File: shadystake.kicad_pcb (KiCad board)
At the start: 2 copper layers, 129.5 x 76.2 mm, 15 parts, among them J1 6P6C, J2 6P6C, J3 6P6C, J4 6P6C, J5 6P6C, J6 6P6C, J7 8P8C

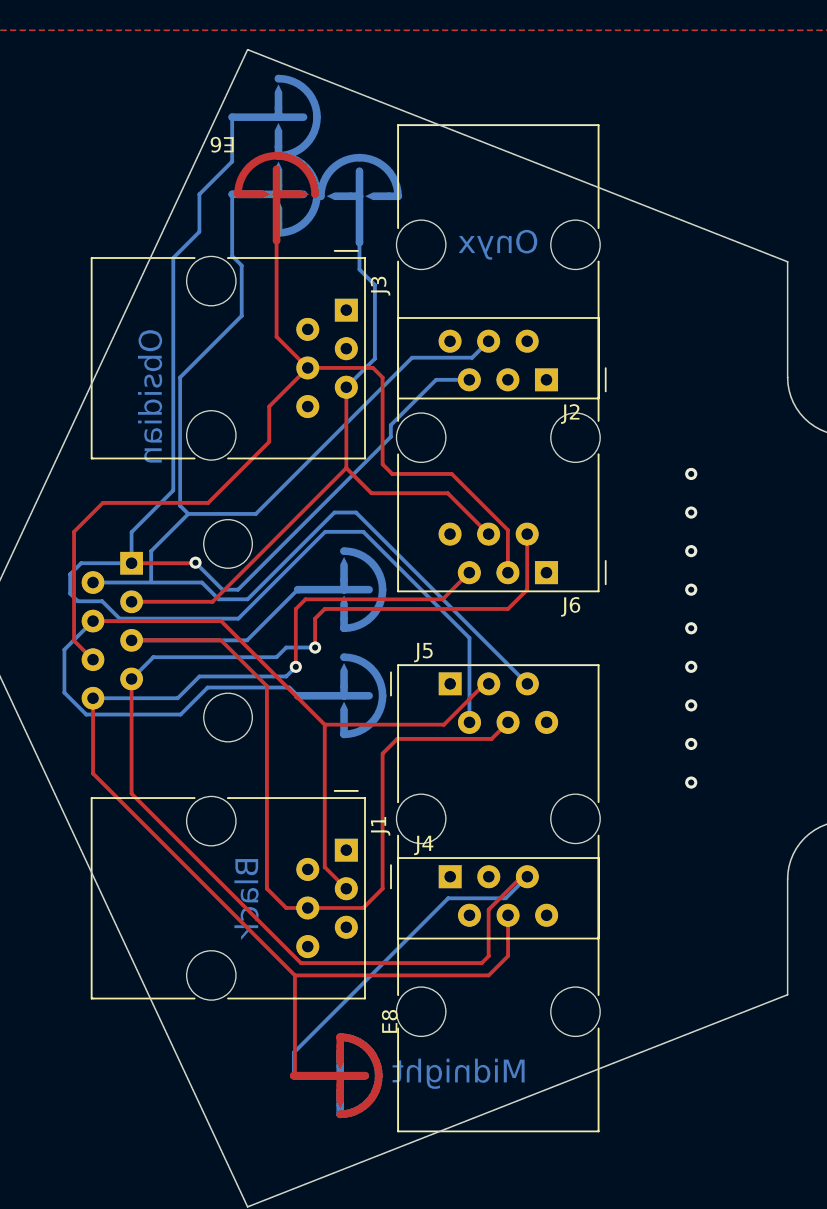
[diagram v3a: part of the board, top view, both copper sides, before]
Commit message: fix spark gaps, continuity on PCB
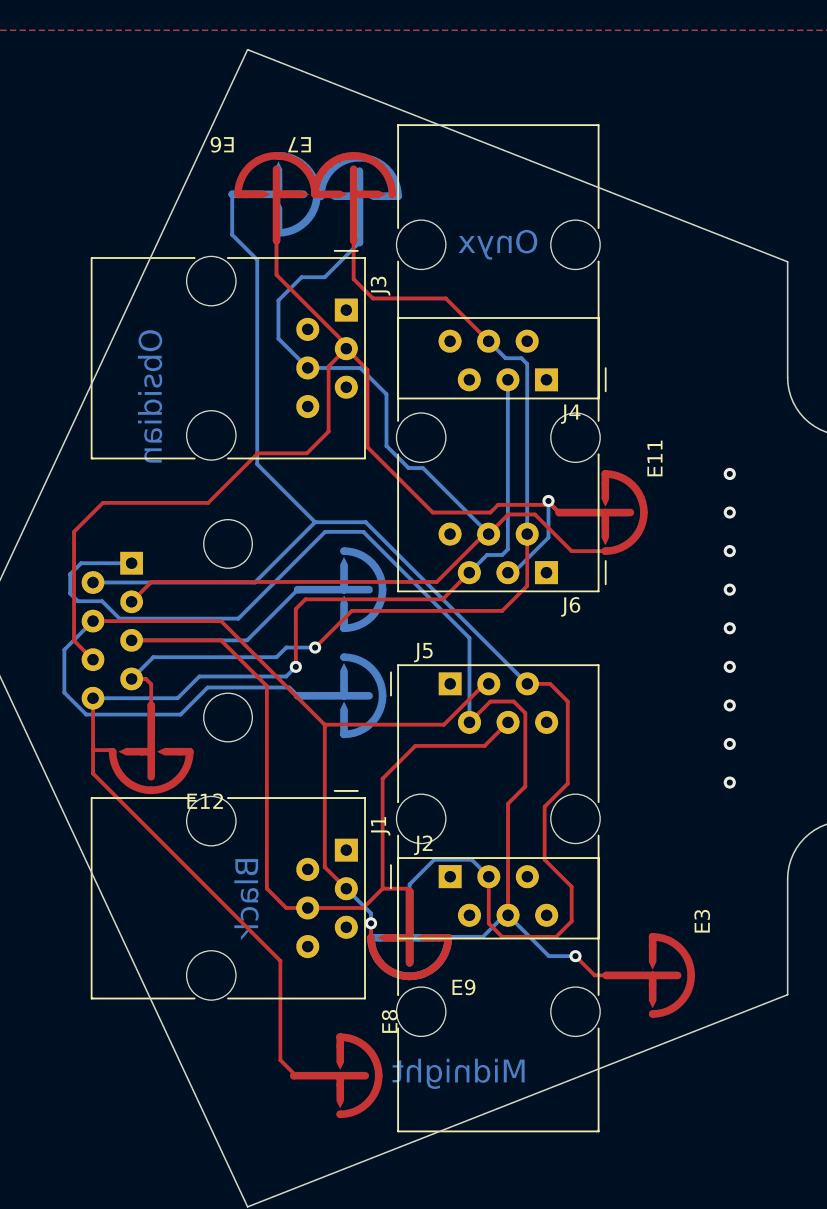
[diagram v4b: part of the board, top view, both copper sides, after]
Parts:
- added E10: SPARK_GAP, Shadystake:Sparkgap_JLC, B.Cu at (76.7, 134.7)
- added E11: SPARK_GAP, Shadystake:Sparkgap_JLC, F.Cu at (89.6, 106.7)
- added E12: SPARK_GAP, Shadystake:Sparkgap_JLC, F.Cu at (59.7, 122.4)
- added E9: SPARK_GAP, Shadystake:Sparkgap_JLC, F.Cu at (76.7, 134.7)
- E3, E7: moved to F.Cu
- moved E3 61.7 mm to (92.7, 137.2), turned to 90 degrees
- moved E7 58.0 mm to (73.0, 85.7), turned to 180 degrees
- moved J2 33.3 mm to (79.4, 130.7), turned to 0 degrees
- moved J4 33.3 mm to (85.7, 97.9), turned to 180 degrees
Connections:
- net GND renamed Earth_Protective
- J2 pad 3: unconnected-(J2-Pad3) -> /RING2
- J2 pad 4: /RING2 -> /TIP2
- J2 pad 5: /TIP2 -> unconnected-(J2-Pad5)
- J3 pad 3: unconnected-(J3-Pad3) -> /RING3
- J3 pad 4: /RING3 -> /TIP3
- J3 pad 5: /TIP3 -> unconnected-(J3-Pad5)
- J4 pad 3: unconnected-(J4-Pad3) -> /RING4
- J4 pad 4: /RING4 -> /TIP4
- J4 pad 5: /TIP4 -> unconnected-(J4-Pad5)
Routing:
- net /TIP4: track 97.0 -> 62.3 mm
- net /TIP2: track 104.7 -> 74.1 mm
- net /TIP3: track 45.0 -> 64.9 mm
- net /RING3: track 63.2 -> 71.7 mm, vias 0 -> 1
- net /RING2: track 89.2 -> 93.6 mm
- net /RING1: track 63.5 -> 67.5 mm, vias 0 -> 1
- net /RING4: track 78.1 -> 76.4 mm
- net /TIP1: track 62.5 -> 63.5 mm

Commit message: Lay out design
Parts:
- E1, E2, E4, E5: footprint Shadystake:Sparkgap_JLC -> Shadystake:Spark_Gap_Teeth; moved to F.Cu
- E10, E3, E6, E7, E8: footprint Shadystake:Sparkgap_JLC -> Shadystake:Spark_Gap_Teeth
- E11, E12, E9: footprint Shadystake:Sparkgap_JLC -> Shadystake:Spark_Gap_Teeth; moved to B.Cu
- J1, J2, J3, J4, J5, J6: footprint Connector_RJ:RJ12_Amphenol_54601 -> Shadystake:6P4C_Vert
- J7: footprint Connector_RJ:RJ45_Amphenol_54602-x08_Horizontal -> Shadystake:8P8C_Hor
- moved E10 104.4 mm to (152.4, 62.7)
- moved J2 103.8 mm to (149.2, 53.9)
- moved J6 98.5 mm to (131.4, 23.4), turned to 0 degrees
- moved E12 98.1 mm to (116.8, 42.7)
- moved J3 97.2 mm to (149.2, 33.6), turned to 0 degrees
- moved J7 91.9 mm to (139.1, 66.0), turned to 180 degrees
- moved J5 90.7 mm to (131.4, 43.7)
- moved E11 89.9 mm to (152.4, 42.4), turned to 180 degrees
- moved J1 85.6 mm to (113.7, 53.9), turned to 0 degrees
- moved E8 84.8 mm to (126.5, 78.7), turned to 0 degrees
- moved E9 82.2 mm to (116.8, 63.0)
- moved E3 76.9 mm to (142.7, 78.7), turned to 180 degrees
- moved E2 74.8 mm to (135.6, 78.7), turned to 0 degrees
- moved E4 72.5 mm to (140.2, 78.7), turned to 0 degrees
- moved J4 70.2 mm to (113.7, 33.6), turned to 0 degrees
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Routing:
- net /RING2: track 93.6 -> 62.7 mm
- net /RING1: track 67.5 -> 84.9 mm, vias 1 -> 0
- net /TIP4: track 62.3 -> 76.7 mm, vias 1 -> 0
- net /TIP1: track 63.5 -> 77.7 mm
- net /TIP3: track 64.9 -> 76.2 mm
- net /TIP2: track 74.1 -> 67.0 mm, vias 1 -> 0
- net /RING4: track 76.4 -> 83.2 mm, vias 1 -> 0
- net /RING3: track 71.7 -> 65.3 mm, vias 1 -> 0
- net Earth_Protective: vias 9 -> 0
- removed copper zone on B.Cu, net Earth_Protective
- removed copper zone on F.Cu, net Earth_Protective
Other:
- board size 129.5 x 76.2 mm -> 96.8 x 67.9 mm
- board text added: "EXPOSED COPPER IS A SAFETY FEATURE DANGER: HIGH VOLTAGE -- DO NOT TOUCH"
- board text added: "FACE TOWARD ENEMY"
- board text removed: "Black"
- board text removed: "Midnight"
- board text removed: "Obsidian"
- board text removed: "Onyx"

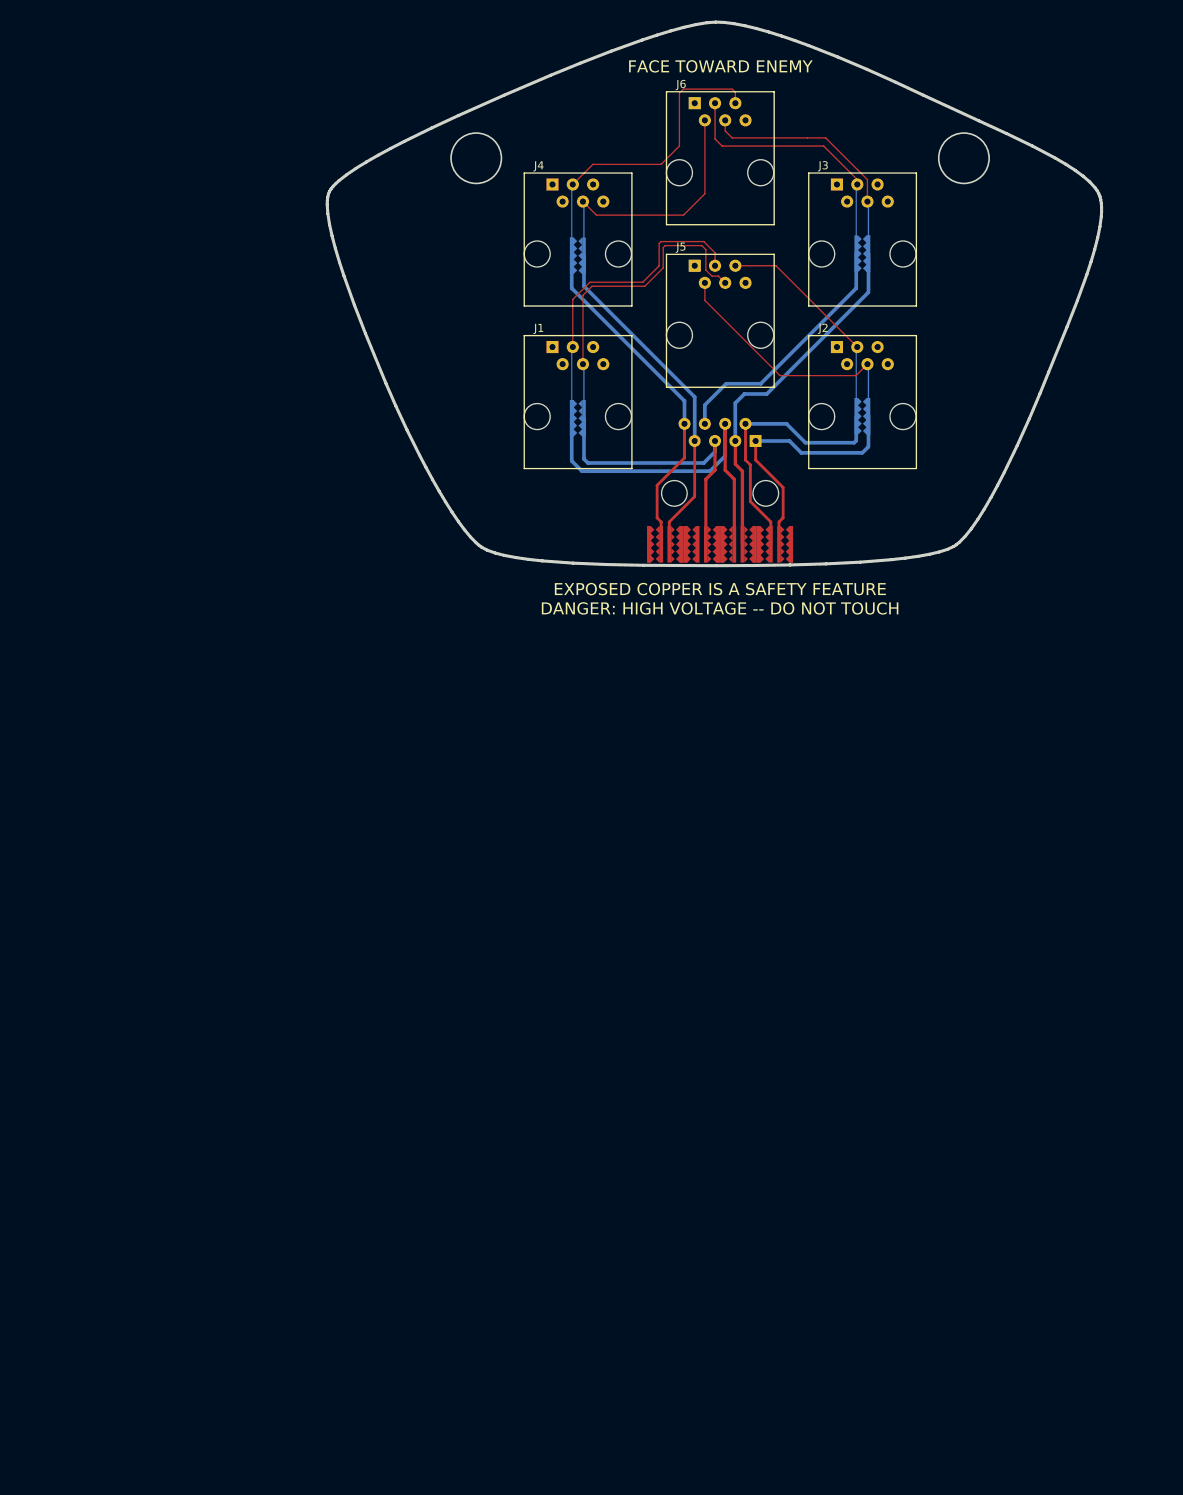
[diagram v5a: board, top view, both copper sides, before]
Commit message: Update design and add footprints
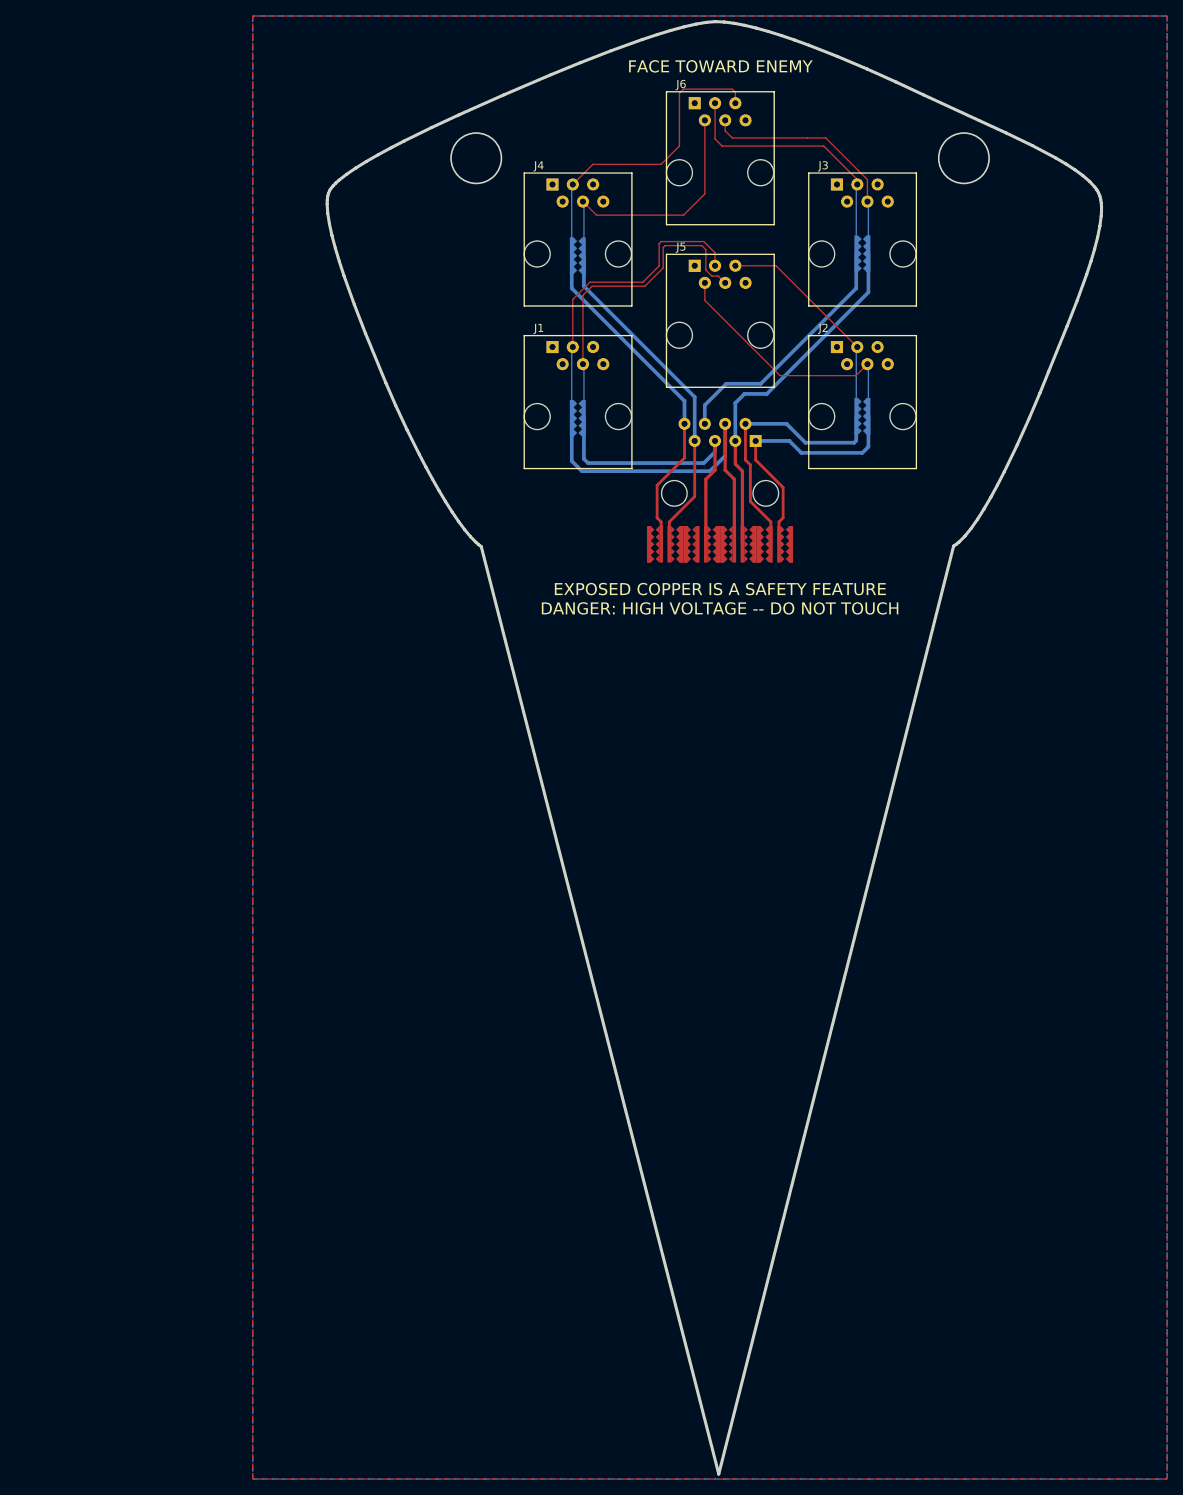
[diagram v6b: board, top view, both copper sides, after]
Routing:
- added copper zone on B.Cu, net Earth_Protective
- added copper zone on F.Cu, net Earth_Protective
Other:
- board size 96.8 x 67.9 mm -> 96.8 x 181.5 mm

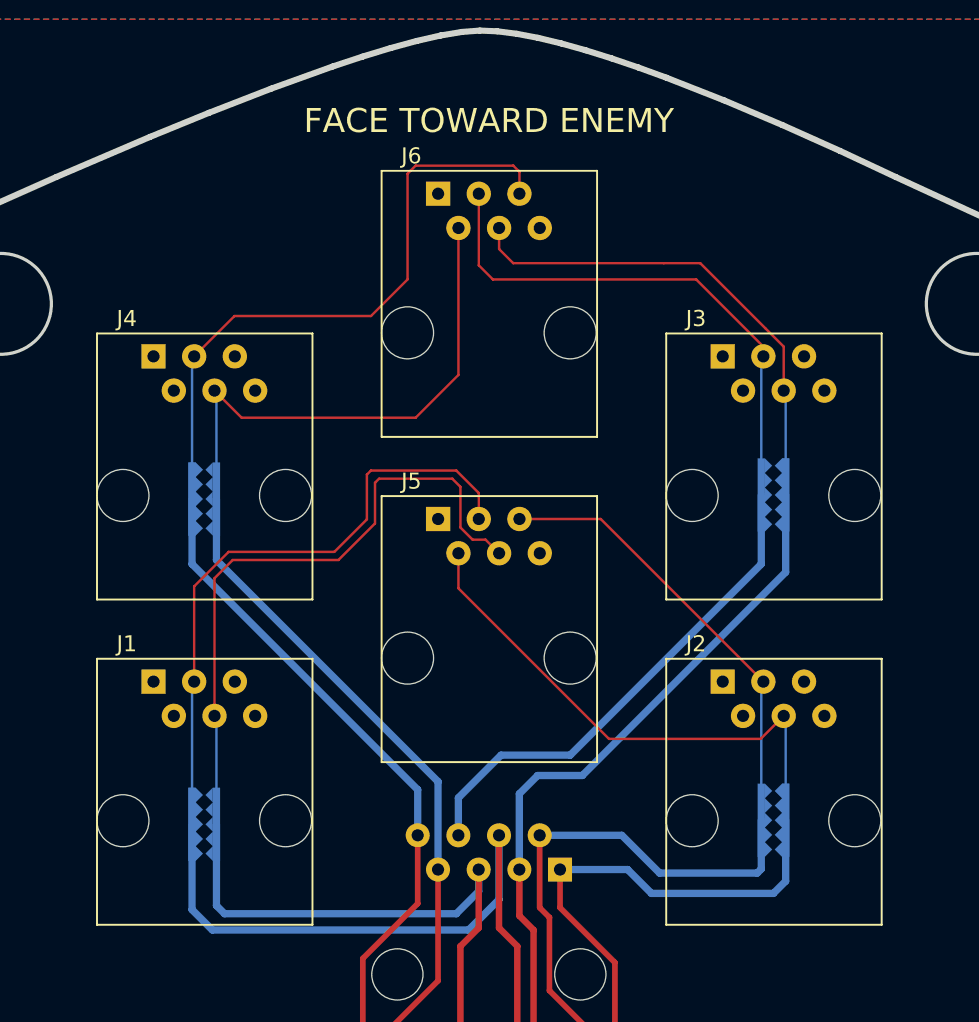
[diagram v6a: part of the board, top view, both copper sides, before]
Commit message: Rotate upper ports by 180 degrees to be compatible with side-insertion jacks
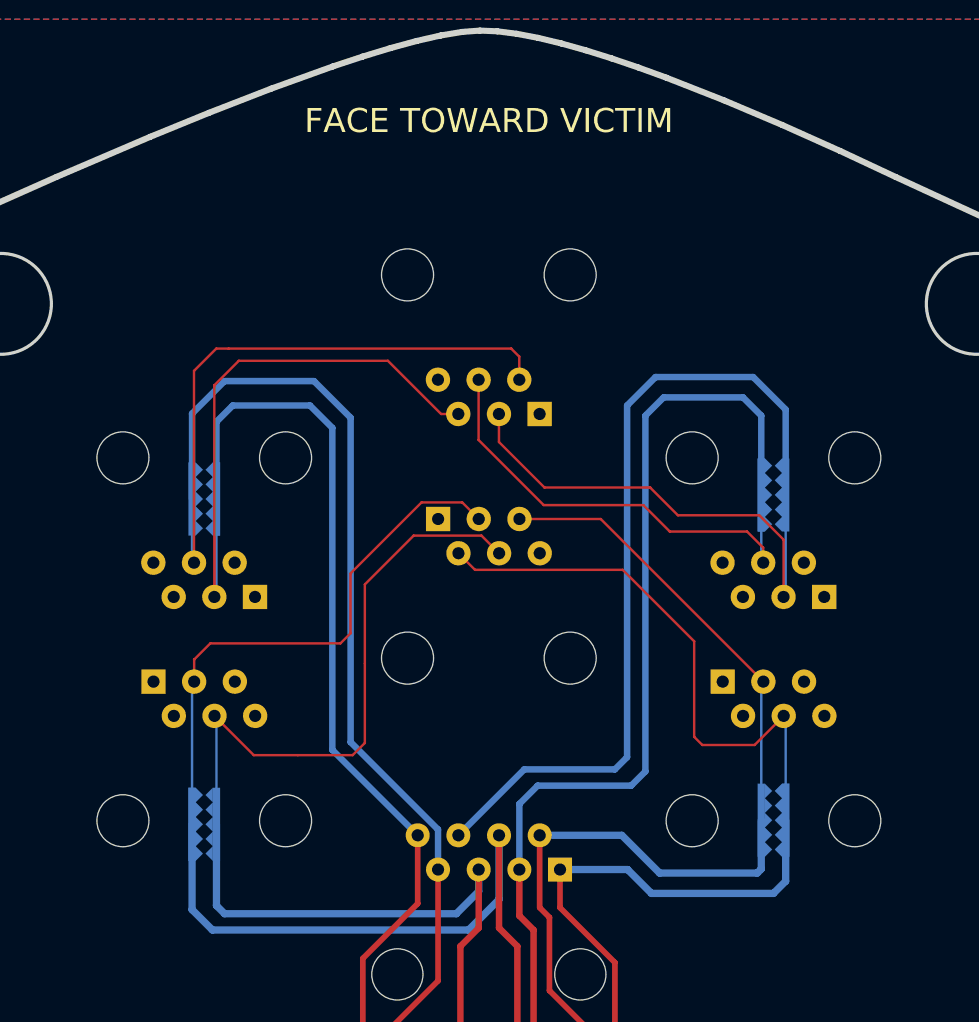
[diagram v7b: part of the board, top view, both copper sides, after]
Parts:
- moved J3 16.7 mm to (155.6, 49.0), turned to 180 degrees
- moved J4 16.7 mm to (120.0, 49.0), turned to 180 degrees
- moved J6 15.5 mm to (137.8, 37.6), turned to 180 degrees
- turned E11 to 0 degrees
- turned E12 to 180 degrees
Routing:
- net /TIP4: track 76.7 -> 100.9 mm
- net /RING3: track 65.3 -> 83.8 mm
- net /TIP3: track 76.2 -> 91.0 mm
- net /RING4: track 83.2 -> 94.1 mm
- net /RING1: track 84.9 -> 80.2 mm
- net /TIP1: track 77.7 -> 74.6 mm
- net /TIP2: track 67.0 -> 69.5 mm
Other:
- board text added: "FACE TOWARD VICTIM"
- board text removed: "FACE TOWARD ENEMY"

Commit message: WTF just happened
Spark gaps are no longer connected to the ground place
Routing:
- net /RING3: track 83.8 -> 99.2 mm
